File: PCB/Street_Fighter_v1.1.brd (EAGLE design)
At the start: 53.3 x 77.5 mm, 49 parts, among them Q1 BSS138, Q2 BSS138, Q3 FQP30N06L, Q4 BSS138, Q5 BSS138, U1 ARDUINO_YUN_SHIELDYUN, U2 MCP6231RT-E/OT

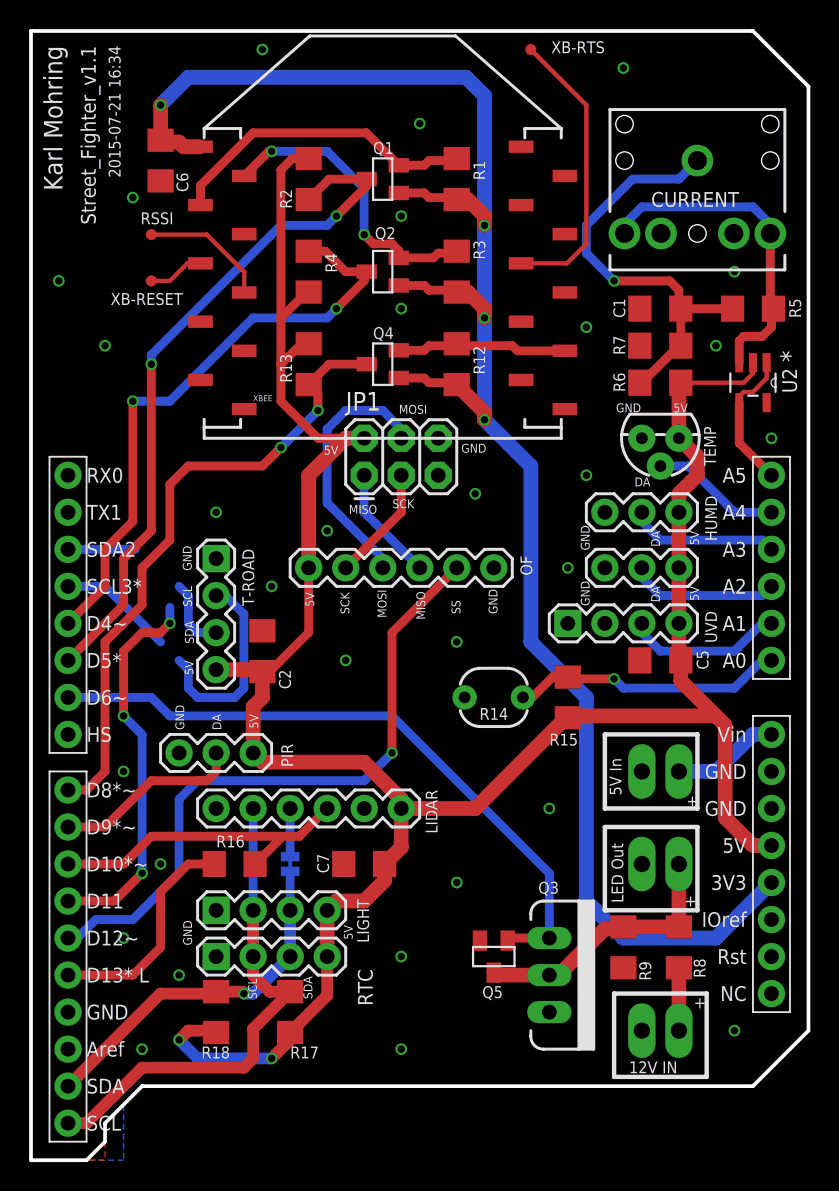
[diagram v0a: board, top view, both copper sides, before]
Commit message: V5 Update
Added 3D printed parts

V5 - Trialling new Sonar detection algorithm
- Sonar must have 2 consecutive detections to register

PIR timeout changed from 5s to 2s.
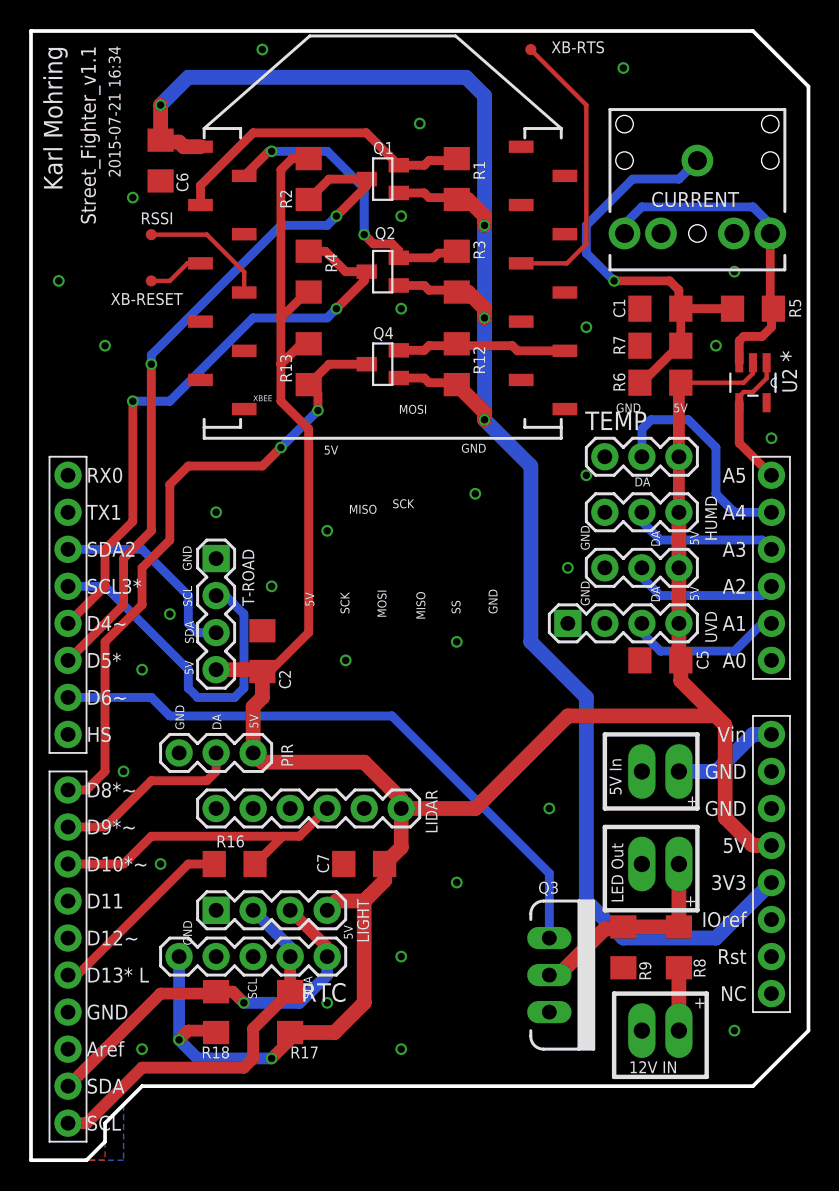
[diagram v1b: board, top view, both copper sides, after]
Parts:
- removed JP1: ICSP Header, SparkFun-Connectors:2X3
- removed OF: ADNS3080, SparkFun-Connectors:1X06
- removed Q5: BSS138, SparkFun-DiscreteSemi:SOT23
- removed R14: PHOTOCELLPTH, SparkFun-Sensors:PHOTOCELL
- removed R15: 10K, SparkFun-Passives:1206
- removed SJ1, SJ2: JUMPER-PAD-2-NC_BY_TRACE, SparkFun-Passives:PAD-JUMPER-2-NC_BY_TRACE_YES_SILK
- RTC: device SparkFun-Connectors:1X04 -> SparkFun-Connectors:1X05
- TEMP: device SparkFun-Sensors:TO-92 -> SparkFun-Connectors:1X03
- moved RTC 7.62 mm to (20.3, 14.0), turned to 180 degrees
- moved TEMP 4.02 mm to (39.4, 48.3), turned to 0 degrees
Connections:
- removed net FLOW-SS: OF.2, U1.12
- removed net LIGHT-STATUS: R14.2, R15.1, U1.A0
- removed net MISO: JP1.1, OF.3
- removed net MLX-PWM: U1.11
- removed net MOSI: JP1.4, OF.4
- removed net SCK: JP1.3, OF.5
- new net SQW: RTC.3
- net +5V: now also RTC.5, TEMP.3; no longer JP1.2, OF.6, R15.2, RTC.4, TEMP.1
- net GND: now also RTC.4, TEMP.1; no longer JP1.6, OF.1, Q5.2, R14.1, RTC.1, TEMP.3
- net LED-CONTROL: no longer Q5.1
- net LED-CONTROL-OUT: no longer Q5.3
- net SCL: no longer LIDAR.2, SJ2.1, SJ2.2
- net SDA: now also RTC.1; no longer LIDAR.3, RTC.3, SJ1.1, SJ1.2
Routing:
- net FLOW-SS: track 45.0 -> 0.00 mm, vias 1 -> 0
- net MLX-PWM: track 26.7 -> 0.00 mm, vias 3 -> 0
- net LIGHT-STATUS: track 18.7 -> 0.00 mm, vias 1 -> 0
- net MOSI: track 17.9 -> 0.00 mm
- net MISO: track 7.93 -> 0.00 mm
- net SCK: track 7.93 -> 0.00 mm
- net SCL: track 34.6 -> 26.8 mm
- net TEMP: track 8.94 -> 15.5 mm
- net SDA@1: track 9.59 -> 13.6 mm
- net LED-CONTROL-OUT: track 18.4 -> 14.5 mm
- net LED-CONTROL: track 45.4 -> 42.5 mm
- net +5V: track 169.5 -> 172.0 mm
- net LIDAR-TRIG: track 15.4 -> 13.2 mm
- net SDA: track 29.2 -> 27.1 mm
- net SCL@1: track 21.9 -> 23.7 mm

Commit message: Removed XBEE API code; now using transparent mode
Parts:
- R5: value 330R -> 2K2
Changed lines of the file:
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@@
 <?xml version="1.0" encoding="utf-8"?>
 <!DOCTYPE eagle SYSTEM "eagle.dtd">
-<eagle version="7.2.0">
+<eagle version="7.5.0">
 <drawing>
 <settings>
@@
 <setting verticaltext="up"/>
 </settings>
-<grid distance="0.025" unitdist="inch" unit="inch" style="lines" multiple="1" display="yes" altdistance="0.005" altunitdist="inch" altunit="inch"/>
+<grid distance="0.05" unitdist="inch" unit="inch" style="lines" multiple="1" display="yes" altdistance="0.005" altunitdist="inch" altunit="inch"/>
 <layers>
 <layer number="1" name="Top" color="4" fill="1" visible="yes" active="yes"/>
@@
 <attribute name="VALUE" x="17.907" y="60.579" size="0.8128" layer="27"/>
 </element>
-<element name="R5" library="SparkFun-Passives" package="1206" value="330R" x="49.53" y="58.42" smashed="yes">
+<element name="R5" library="SparkFun-Passives" package="1206" value="2K2 " x="49.53" y="58.42" smashed="yes">
 <attribute name="NAME" x="52.832" y="57.785" size="0.8128" layer="25" rot="R90"/>
 <attribute name="VALUE" x="49.911" y="57.15" size="0.8128" layer="27" rot="R90"/>
